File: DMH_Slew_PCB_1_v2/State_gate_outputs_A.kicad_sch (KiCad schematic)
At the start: 26 parts, among them J4 TS_Jack_6.35mm_Sw, J5 TS_Jack_6.35mm_Sw, J51 Conn_01x08_PinHeader, Q5 BC548, Q6 BC548, U1 TL074

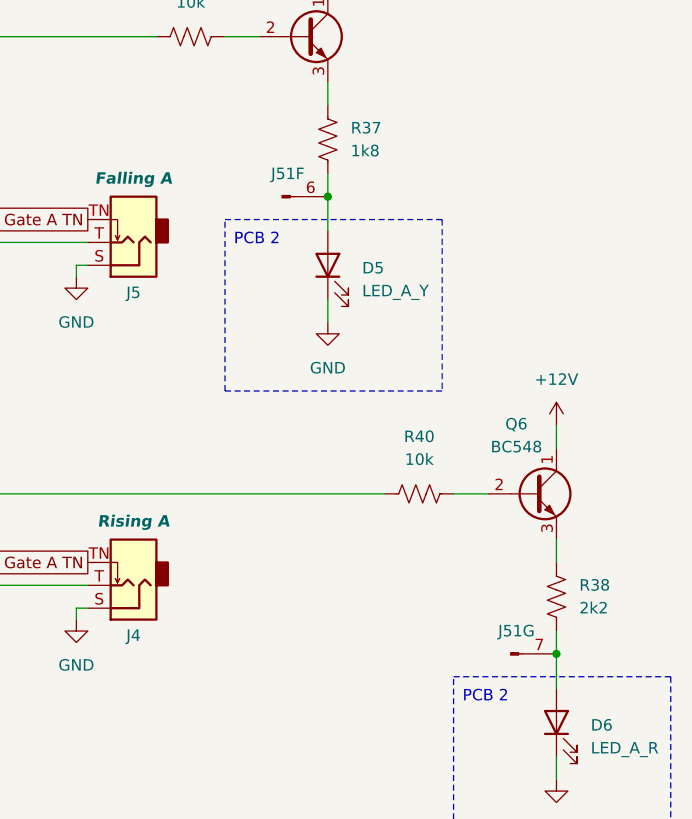
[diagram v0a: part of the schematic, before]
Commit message: PCB 2 component placement done
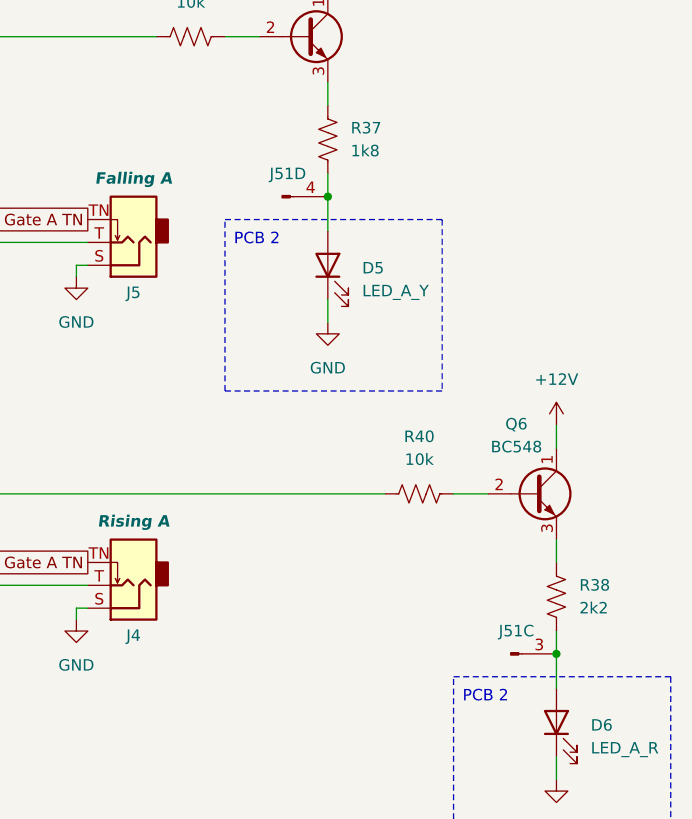
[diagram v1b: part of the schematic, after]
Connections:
- net at D6.2 (A), R38.2: now also J51.3 (Pin_3); no longer J51.7 (Pin_7)
- net at D5.2 (A), R37.2: now also J51.4 (Pin_4); no longer J51.6 (Pin_6)
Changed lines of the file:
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@@
 		(lib_id "SynthStuff:Conn_01x08_PinHeader")
 		(at 251.46 106.68 0)
-		(unit 7)
+		(unit 3)
 		(exclude_from_sim no)
 		(in_bom yes)
@@
 			)
 		)
+		(property "Function" ""
+			(at 251.46 106.68 0)
+			(effects
+				(font
+					(size 1.27 1.27)
+				)
+			)
+		)
 		(pin "3"
 		)
@@
 				(path "/58f4306d-5387-4983-bb08-41a2313fd315/695faa68-e325-44bd-a237-dc69a864c9b9"
 					(reference "J51")
-					(unit 7)
+					(unit 3)
 				)
 			)
@@
 		(lib_id "SynthStuff:Conn_01x08_PinHeader")
 		(at 226.06 55.88 0)
-		(unit 6)
+		(unit 4)
 		(exclude_from_sim no)
 		(in_bom yes)
@@
 			)
 		)
+		(property "Function" ""
+			(at 226.06 55.88 0)
+			(effects
+				(font
+					(size 1.27 1.27)
+				)
+			)
+		)
 		(pin "3"
 		)
@@
 				(path "/58f4306d-5387-4983-bb08-41a2313fd315/695faa68-e325-44bd-a237-dc69a864c9b9"
 					(reference "J51")
-					(unit 6)
-				)
-			)
+					(unit 4)
+				)
+			)

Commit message: PCB 1 component placement ongoing
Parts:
- Q6: footprint Package_TO_SOT_THT:TO-92_Inline -> Package_TO_SOT_THT:TO-92L_Inline_Wide
- U1: footprint Package_DIP:DIP-16_W7.62mm_Socket -> Package_DIP:DIP-14_W7.62mm_Socket
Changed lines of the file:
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@@
 			)
 		)
-		(property "Footprint" "Package_DIP:DIP-16_W7.62mm_Socket"
+		(property "Footprint" "Package_DIP:DIP-14_W7.62mm_Socket"
 			(at 151.13 101.6 0)
 			(effects
@@
 			)
 		)
-		(property "Footprint" "Package_DIP:DIP-16_W7.62mm_Socket"
+		(property "Footprint" "Package_DIP:DIP-14_W7.62mm_Socket"
 			(at 62.23 78.74 0)
 			(effects
@@
 			)
 		)
-		(property "Footprint" "Package_TO_SOT_THT:TO-92_Inline"
+		(property "Footprint" "Package_TO_SOT_THT:TO-92L_Inline_Wide"
 			(at 259.08 90.805 0)
 			(effects
@@
 			)
 		)
-		(property "Footprint" "Package_DIP:DIP-16_W7.62mm_Socket"
+		(property "Footprint" "Package_DIP:DIP-14_W7.62mm_Socket"
 			(at 151.13 58.42 0)
 			(effects
